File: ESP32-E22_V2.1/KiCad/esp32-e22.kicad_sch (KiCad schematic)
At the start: 32 parts, among them J1 Conn_01x04_Socket, J10 Conn_01x02_Socket, J3 Conn_01x04_Socket, J4 Conn_01x03_Socket, J5 SMA, J6 Conn_01x02_Socket, J7 USB_C_Receptacle_PowerOnly_6P, J8 Conn_01x04_Socket, J9 Conn_01x02_Socket, SW1 SW_Push, U1 E22-40033S, U2 ESP32-DevKitC, U3 DM-OLED096-636

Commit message: new Version 2.0.10 & 2.0.6
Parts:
- removed J7: USB_C_Receptacle_PowerOnly_6P, Connector_USB:USB_C_Receptacle_GCT_USB4125-xx-x-0190_6P_TopMnt_Horizontal, symbol Connector:USB_C_Receptacle_PowerOnly_6P
- added J2: Conn_01x04_Socket, Connector_PinHeader_2.54mm:PinHeader_1x04_P2.54mm_Vertical, symbol Connector:Conn_01x04_Socket
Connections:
- net +5V: now also D2.1 (A1); no longer D2.2 (A2)
- net GND: now also D2.2 (A2), J2.4 (Pin_4); no longer D2.1 (A1)
- net at R2.1: now also J2.2 (Pin_2)
- net at D3.2 (A): now also J2.1 (Pin_1)
- net at R1.1: now also J2.3 (Pin_3)
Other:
- moved on the sheet: D2
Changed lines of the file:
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@@
 		(title "ESP32 - E22 Board")
 		(date "2024-10-04")
-		(rev "V2.0.9")
+		(rev "V2.0.10")
 		(company "DK9BT / OE3WAS")
 	)
@@
 	)
 	(junction
-		(at 31.75 181.61)
-		(diameter 0)
-		(color 0 0 0 0)
-	)
-	(junction
 		(at 81.28 156.21)
 		(diameter 0)
@@
 	)
 	(junction
-		(at 175.26 93.98)
+		(at 86.36 181.61)
 		(diameter 0)
 		(color 0 0 0 0)
 	)
 	(junction
-		(at 99.06 26.67)
+		(at 175.26 93.98)
 		(diameter 0)
 		(color 0 0 0 0)
 	)
 	(junction
-		(at 40.64 181.61)
+		(at 99.06 26.67)
 		(diameter 0)
 		(color 0 0 0 0)
@@
 	(wire
 		(pts
+			(xy 40.64 165.1) (xy 46.99 171.45)
+		)
+		(stroke
+			(width 0)
+			(type default)
+		)
+	)
+	(wire
+		(pts
 			(xy 143.51 165.1) (xy 143.51 168.91)
 		)
@@
 	(wire
 		(pts
-			(xy 49.53 181.61) (xy 40.64 181.61)
+			(xy 25.4 49.53) (xy 35.56 49.53)
 		)
 		(stroke
@@
 	(wire
 		(pts
-			(xy 25.4 49.53) (xy 35.56 49.53)
+			(xy 198.12 55.88) (xy 223.52 55.88)
 		)
 		(stroke
@@
 	(wire
 		(pts
-			(xy 198.12 55.88) (xy 223.52 55.88)
+			(xy 246.38 48.26) (xy 254 48.26)
 		)
 		(stroke
@@
 	(wire
 		(pts
-			(xy 246.38 48.26) (xy 254 48.26)
+			(xy 119.38 156.21) (xy 132.08 156.21)
 		)
 		(stroke
@@
 	(wire
 		(pts
-			(xy 119.38 156.21) (xy 132.08 156.21)
+			(xy 154.94 44.45) (xy 154.94 43.18)
 		)
 		(stroke
@@
 	(wire
 		(pts
-			(xy 154.94 44.45) (xy 154.94 43.18)
+			(xy 128.27 50.8) (xy 190.5 50.8)
 		)
 		(stroke
@@
 	(wire
 		(pts
-			(xy 128.27 50.8) (xy 190.5 50.8)
+			(xy 132.08 168.91) (xy 143.51 168.91)
 		)
 		(stroke
@@
 	(wire
 		(pts
-			(xy 132.08 168.91) (xy 143.51 168.91)
+			(xy 38.1 165.1) (xy 40.64 165.1)
 		)
 		(stroke
@@
 	(wire
 		(pts
+			(xy 38.1 172.72) (xy 46.99 181.61)
+		)
+		(stroke
+			(width 0)
+			(type default)
+		)
+	)
+	(wire
+		(pts
 			(xy 248.92 66.04) (xy 248.92 76.2)
 		)
@@
 	(wire
 		(pts
-			(xy 40.64 181.61) (xy 40.64 184.15)
+			(xy 86.36 181.61) (xy 86.36 182.88)
 		)
 		(stroke
@@
 	(wire
 		(pts
+			(xy 86.36 181.61) (xy 58.42 181.61)
+		)
+		(stroke
+			(width 0)
+			(type default)
+		)
+	)
+	(wire
+		(pts
 			(xy 260.35 58.42) (xy 260.35 60.96)
 		)
@@
 	(wire
 		(pts
-			(xy 24.13 181.61) (xy 31.75 181.61)
+			(xy 46.99 181.61) (xy 49.53 181.61)
 		)
 		(stroke
@@
 	(wire
 		(pts
+			(xy 38.1 162.56) (xy 40.64 162.56)
+		)
+		(stroke
+			(width 0)
+			(type default)
+		)
+	)
+	(wire
+		(pts
 			(xy 128.27 48.26) (xy 195.58 48.26)
 		)
@@
 	(wire
 		(pts
-			(xy 119.38 168.91) (xy 132.08 168.91)
+			(xy 38.1 167.64) (xy 38.1 172.72)
 		)
 		(stroke
@@
 	(wire
 		(pts
-			(xy 246.38 78.74) (xy 248.92 78.74)
+			(xy 119.38 168.91) (xy 132.08 168.91)
 		)
 		(stroke
@@
 	(wire
 		(pts
-			(xy 58.42 181.61) (xy 119.38 181.61)
+			(xy 246.38 78.74) (xy 248.92 78.74)
 		)
 		(stroke
@@
 	(wire
 		(pts
+			(xy 38.1 160.02) (xy 43.18 160.02)
+		)
+		(stroke
+			(width 0)
+			(type default)
+		)
+	)
+	(wire
+		(pts
 			(xy 154.94 44.45) (xy 158.75 44.45)
 		)
@@
 	(wire
 		(pts
+			(xy 86.36 181.61) (xy 119.38 181.61)
+		)
+		(stroke
+			(width 0)
+			(type default)
+		)
+	)
+	(wire
+		(pts
 			(xy 71.12 162.56) (xy 72.39 162.56)
 		)
@@
 	(wire
 		(pts
+			(xy 40.64 162.56) (xy 46.99 168.91)
+		)
+		(stroke
+			(width 0)
+			(type default)
+		)
+	)
+	(wire
+		(pts
 			(xy 220.98 81.28) (xy 220.98 82.55)
 		)
@@
 	(wire
 		(pts
-			(xy 31.75 181.61) (xy 40.64 181.61)
-		)
-		(stroke
-			(width 0)
-			(type default)
-		)
-	)
-	(wire
-		(pts
 			(xy 195.58 66.04) (xy 223.52 66.04)
 		)
@@
 	(wire
 		(pts
+			(xy 43.18 160.02) (xy 46.99 156.21)
+		)
+		(stroke
+			(width 0)
+			(type default)
+		)
+	)
+	(wire
+		(pts
 			(xy 175.26 78.74) (xy 185.42 78.74)
 		)
@@
 	)
 	(symbol
-		(lib_id "Connector:USB_C_Receptacle_PowerOnly_6P")
-		(at 31.75 163.83 0)
-		(unit 1)
-		(exclude_from_sim no)
-		(in_bom yes)
-		(on_board yes)
-		(dnp no)
-		(fields_autoplaced yes)
-		(property "Reference" "J7"
-			(at 31.75 148.59 0)
-			(effects
-				(font
-					(size 1.27 1.27)
-				)
-			)
-		)
-		(property "Value" "USB_C_Receptacle_PowerOnly_6P"
-			(at 31.75 148.59 0)
-			(effects
-				(font
-					(size 1.27 1.27)
-				)
-				(hide yes)
-			)
-		)
-		(property "Footprint" "Connector_USB:USB_C_Receptacle_GCT_USB4125-xx-x-0190_6P_TopMnt_Horizontal"
-			(at 35.56 161.29 0)
-			(effects
-				(font
-					(size 1.27 1.27)
-				)
-				(hide yes)
-			)
-		)
-		(property "Datasheet" "https://www.usb.org/sites/default/files/documents/usb_type-c.zip"
-			(at 31.75 163.83 0)
-			(effects
-				(font
-					(size 1.27 1.27)
-				)
-				(hide yes)
-			)
-		)
-		(property "Description" "USB Power-Only 6P Type-C Receptacle connector"
-			(at 31.75 163.83 0)
-			(effects
-				(font
-					(size 1.27 1.27)
-				)
-				(hide yes)
-			)
-		)
-		(pin "A12"
-		)
-		(pin "S1"
-		)
-		(pin "A9"
-		)
-		(pin "B5"
-		)
-		(pin "B9"
-		)
-		(pin "B12"
-		)
-		(pin "A5"
-		)
-		(instances
-			(project ""
-				(path "/7ac59502-473d-4014-a9ef-f4cf3cefb926"
-					(reference "J7")
-					(unit 1)
-				)
-			)
-		)
-	)
-	(symbol
 		(lib_id "Device:R")
 		(at 30.48 38.1 90)
@@
 	)
 	(symbol
+		(lib_id "Connector:Conn_01x04_Socket")
+		(at 33.02 162.56 0)
+		(mirror y)
+		(unit 1)
+		(exclude_from_sim no)
+		(in_bom yes)
+		(on_board yes)
+		(dnp no)
+		(property "Reference" "J2"
+			(at 34.29 169.926 0)
+			(effects
+				(font
+					(size 1.27 1.27)
+				)
+				(justify left)
+			)
+		)
+		(property "Value" "Conn_01x04_Socket"
+			(at 26.162 165.1 0)
+			(effects
+				(font
+					(size 1.27 1.27)
+				)
+				(justify left)
+				(hide yes)
+			)
+		)
+		(property "Footprint" "Connector_PinHeader_2.54mm:PinHeader_1x04_P2.54mm_Vertical"
+			(at 33.02 162.56 0)
+			(effects
+				(font
+					(size 1.27 1.27)
+				)
+				(hide yes)
+			)
+		)
+		(property "Datasheet" "~"
+			(at 33.02 162.56 0)
+			(effects
+				(font
+					(size 1.27 1.27)
+				)
+				(hide yes)
+			)
+		)
+		(property "Description" "Generic connector, single row, 01x04, script generated"
+			(at 33.02 162.56 0)
+			(effects
+				(font
+					(size 1.27 1.27)
+				)
+				(hide yes)
+			)
+		)
+		(pin "1"
+		)
+		(pin "4"
+		)
+		(pin "3"
+		)
+		(pin "2"
+		)
+		(instances
+			(project "esp32-e22"
+				(path "/7ac59502-473d-4014-a9ef-f4cf3cefb926"
+					(reference "J2")
+					(unit 1)
+				)
+			)
+		)
+	)
+	(symbol
 		(lib_id "power:+3.3V")
 		(at 99.06 26.67 0)
@@
 	(symbol
 		(lib_id "Diode:SD05_SOD323")
-		(at 86.36 162.56 90)
+		(at 86.36 162.56 270)
 		(unit 1)
 		(exclude_from_sim no)
@@
 					(size 1.27 1.27)
 				)
-				(justify right)
+				(justify left)
 			)
 		)
@@
 					(size 1.27 1.27)
 				)
-				(justify right)
+				(justify left)
 			)
 		)
 		(property "Footprint" "Diode_SMD:D_SOD-523"
-			(at 91.44 162.56 0)
+			(at 81.28 162.56 0)
 			(effects
 				(font
@@
 	(symbol
 		(lib_id "power:GND")
-		(at 40.64 184.15 0)
+		(at 86.36 182.88 0)
 		(unit 1)
 		(exclude_from_sim no)
@@
 		(fields_autoplaced yes)
 		(property "Reference" "#PWR021"
-			(at 40.64 190.5 0)
+			(at 86.36 189.23 0)
 			(effects
 				(font
@@
 		)
 		(property "Value" "GND"
-			(at 40.64 189.23 0)
+			(at 86.36 187.96 0)
 			(effects
 				(font
@@
 		)
 		(property "Footprint" ""
-			(at 40.64 184.15 0)
+			(at 86.36 182.88 0)
 			(effects
 				(font
@@
 		)
 		(property "Datasheet" ""
-			(at 40.64 184.15 0)
+			(at 86.36 182.88 0)
 			(effects
 				(font
@@
 		)
 		(property "Description" "Power symbol creates a global label with name \"GND\" , ground"
-			(at 40.64 184.15 0)
+			(at 86.36 182.88 0)
 			(effects
 				(font

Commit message: real update
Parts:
- removed J2: Conn_01x04_Socket, Connector_PinHeader_2.54mm:PinHeader_1x04_P2.54mm_Vertical, symbol Connector:Conn_01x04_Socket
- added C8: 100nF, Capacitor_THT:C_Disc_D4.7mm_W2.5mm_P5.00mm, symbol Device:C_Small
- added J2: ~, footprints:USB-C_vert, symbol USB-C:USB-C_vert
- added R8: 0R, Resistor_SMD:R_0805_2012Metric, symbol Device:R
- J3: renamed from J9; Funktion (none) -> ext. Power 5V DC
- J4: renamed from J1; Funktion (none) -> GPS
- J5: renamed from J4; Funktion (none) -> ONEWIRE
- J6: renamed from J8; Funktion (none) -> I²C
- J7: renamed from J3; Funktion (none) -> I²C
- J8: renamed from J5; Funktion (none) -> Antenne
- renumbered C5 to C1, C6 to C2, C1 to C3, C2 to C4, C3 to C5, C7 to C6, C4 to C7, D3 to D1, D1 to D2, D2 to D3, J10 to J1, J6 to J9, R3 to R1, R4 to R2, R1 to R3, R2 to R4, U2 to U1, U3 to U2, U1 to U3
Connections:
- net +3.3V: now also C8.2
- net GND: now also C8.1, J2.4 (GND)
- net at R3.1: now also J2.3 (CC2)
- net at D1.2 (A): now also J2.1 (V+)
- net at R4.1: now also J2.2 (CC1)
- net at J8.1 (In): now also R8.1; no longer U3.21 (ANT)
- new net: R8.2, U3.21 (ANT)
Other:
- note removed: "BME"
- note removed: "GPS"
- note removed: "ONEWIRE"
- note removed: "ext. Power 5V DC"
- moved on the sheet: J8, J9, R3, R4, U3

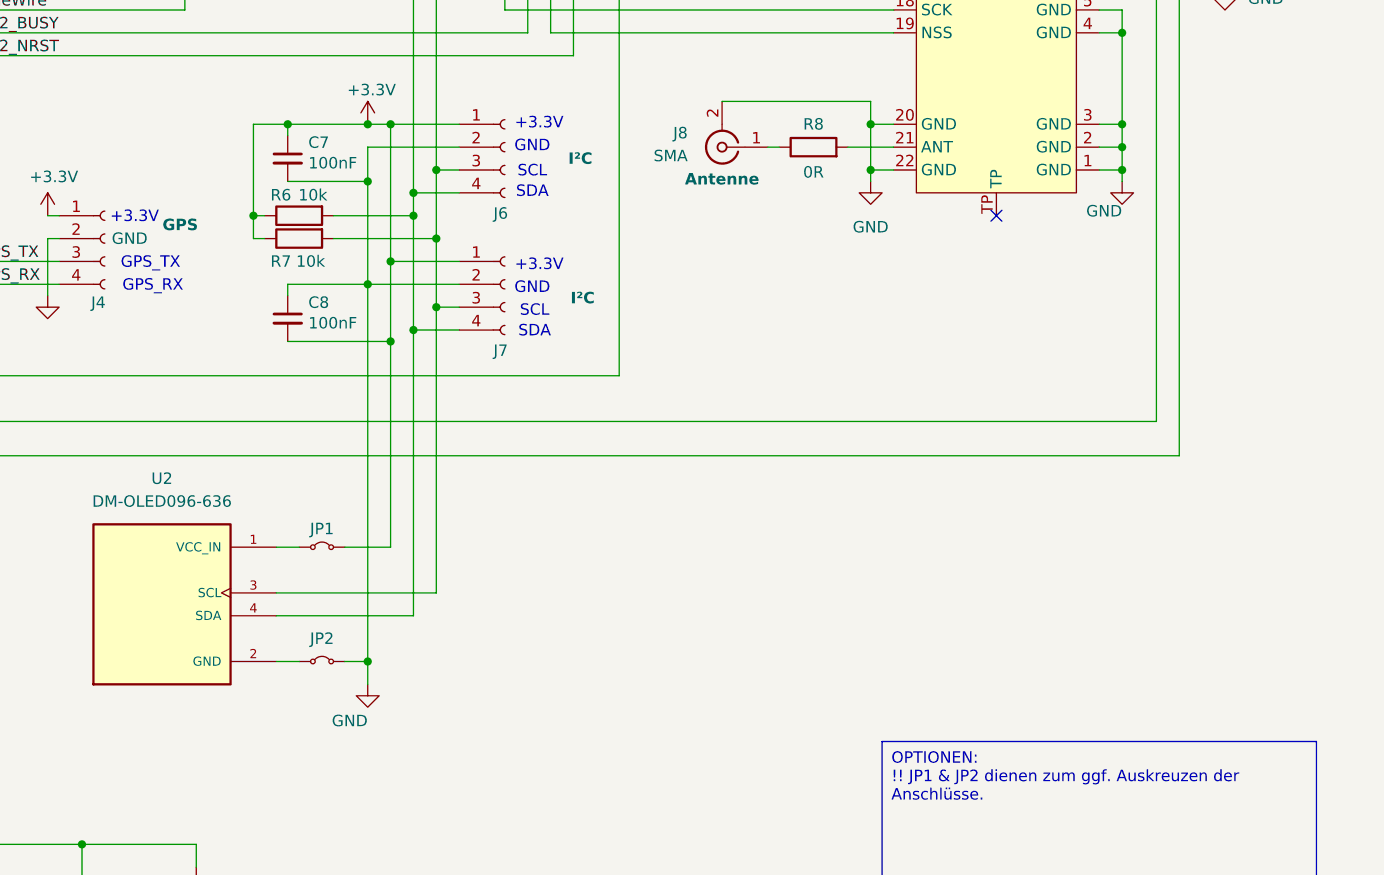
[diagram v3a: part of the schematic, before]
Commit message: corrected footprints symbols and 3d Models for our custom parts
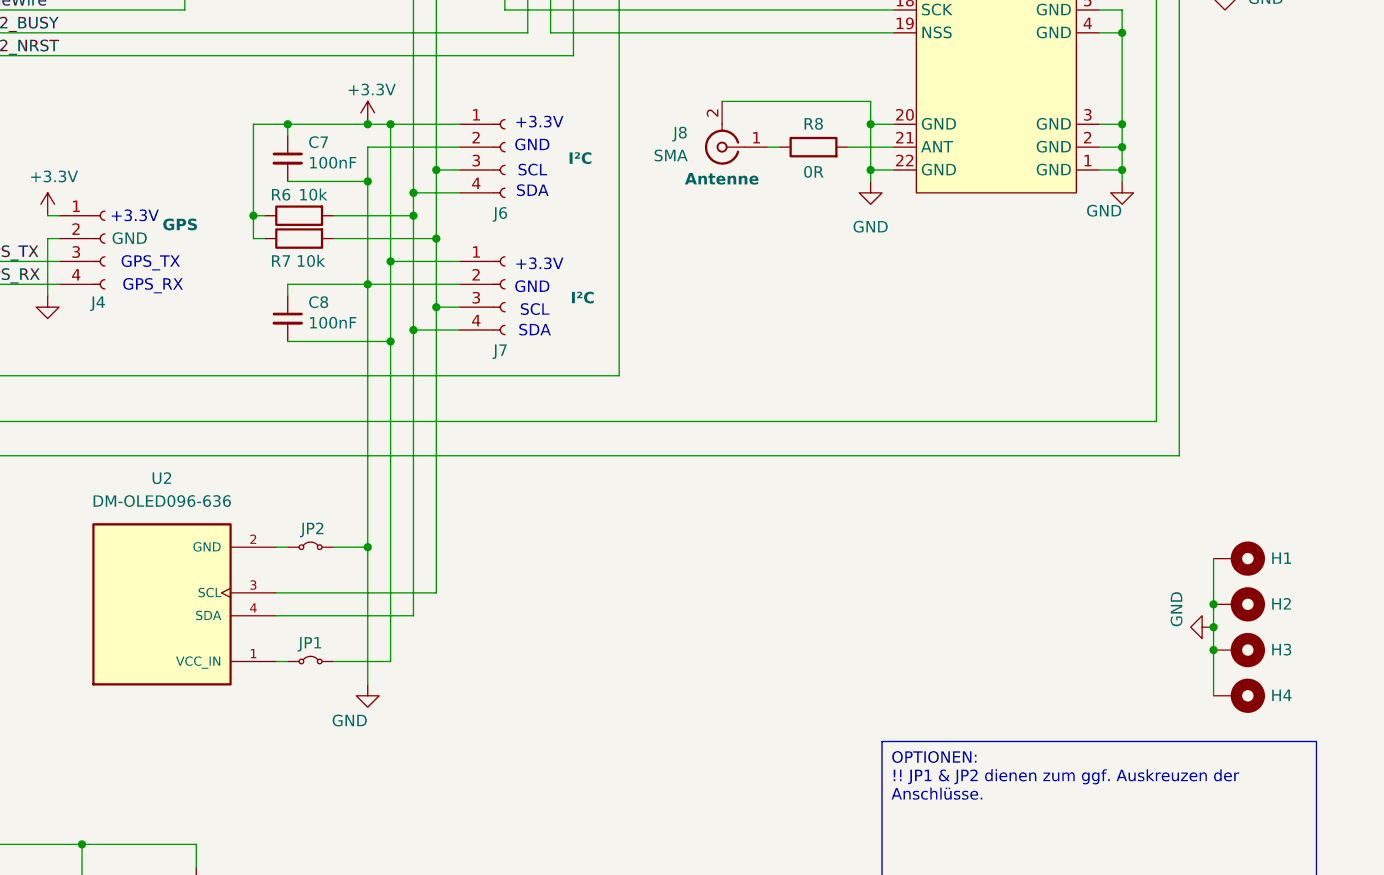
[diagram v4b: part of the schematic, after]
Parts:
- added H1, H2, H3, H4: MountingHole_Pad, MountingHole:MountingHole_2.2mm_M2_Pad_TopBottom, symbol Mechanical:MountingHole_Pad
- J2: footprint footprints:USB-C_vert -> footprints_local:USB-C_vert
- U1: footprint E22:ESP32-DevKitC -> footprints_local:ESP32-DevKitC
- U2: footprint E22:DM-OLED096-636 -> footprints_local:DM-OLED096-636
- U3: footprint E22:E22-400M33S -> footprints_local:E22-400M33S
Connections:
- net GND: now also H1.1, H2.1, H3.1, H4.1
- no-connect marks 17 -> 16
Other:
- moved on the sheet: JP1, JP2

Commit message: some fixes
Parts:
- added NT1: NetTie_2, NetTie:NetTie-2_SMD_Pad0.5mm, symbol NetTie:NetTie_2
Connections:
- net +3.3V: now also JP1.1 (A), U2.1 (VCC_IN)
- net GND: now also NT1.2; no longer JP2.2 (B)
- net at JP2.1 (A), U2.2 (GND): now also JP2.2 (B), NT1.1
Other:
- moved on the sheet: JP2
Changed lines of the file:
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@@
 	)
 	(junction
+		(at 171.45 135.89)
+		(diameter 0)
+		(color 0 0 0 0)
+	)
+	(junction
 		(at 182.88 96.52)
 		(diameter 0)
@@
 	)
 	(junction
+		(at 175.26 123.19)
+		(diameter 0)
+		(color 0 0 0 0)
+	)
+	(junction
 		(at 81.28 156.21)
 		(diameter 0)
@@
 	)
 	(junction
+		(at 165.1 123.19)
+		(diameter 0)
+		(color 0 0 0 0)
+	)
+	(junction
 		(at 180.34 99.06)
 		(diameter 0)
@@
 	)
 	(junction
+		(at 170.18 123.19)
+		(diameter 0)
+		(color 0 0 0 0)
+	)
+	(junction
 		(at 86.36 156.21)
 		(diameter 0)
@@
 	)
 	(junction
+		(at 166.37 135.89)
+		(diameter 0)
+		(color 0 0 0 0)
+	)
+	(junction
 		(at 259.08 66.04)
 		(diameter 0)
@@
 	)
 	(junction
-		(at 175.26 123.19)
-		(diameter 0)
-		(color 0 0 0 0)
-	)
-	(junction
 		(at 269.24 134.62)
 		(diameter 0)
@@
 	(wire
 		(pts
+			(xy 170.18 123.19) (xy 170.18 124.46)
+		)
+		(stroke
+			(width 0)
+			(type default)
+		)
+	)
+	(wire
+		(pts
 			(xy 166.37 93.98) (xy 175.26 93.98)
 		)
@@
 	(wire
 		(pts
+			(xy 171.45 137.16) (xy 171.45 135.89)
+		)
+		(stroke
+			(width 0)
+			(type default)
+		)
+	)
+	(wire
+		(pts
 			(xy 49.53 33.02) (xy 52.07 33.02)
 		)
@@
 	(wire
 		(pts
+			(xy 165.1 124.46) (xy 170.18 124.46)
+		)
+		(stroke
+			(width 0)
+			(type default)
+		)
+	)
+	(wire
+		(pts
 			(xy 81.28 156.21) (xy 86.36 156.21)
 		)
@@
 	(wire
 		(pts
-			(xy 165.1 123.19) (xy 166.37 123.19)
-		)
-		(stroke
-			(width 0)
-			(type default)
-		)
-	)
-	(wire
-		(pts
 			(xy 180.34 83.82) (xy 180.34 86.36)
 		)
@@
 	(wire
 		(pts
+			(xy 175.26 123.19) (xy 175.26 138.43)
+		)
+		(stroke
+			(width 0)
+			(type default)
+		)
+	)
+	(wire
+		(pts
 			(xy 156.21 166.37) (xy 156.21 168.91)
 		)
@@
 	(wire
 		(pts
+			(xy 165.1 123.19) (xy 165.1 124.46)
+		)
+		(stroke
+			(width 0)
+			(type default)
+		)
+	)
+	(wire
+		(pts
 			(xy 36.83 156.21) (xy 49.53 156.21)
 		)
@@
 	(wire
 		(pts
-			(xy 175.26 123.19) (xy 175.26 138.43)
-		)
-		(stroke
-			(width 0)
-			(type default)
-		)
-	)
-	(wire
-		(pts
 			(xy 203.2 50.8) (xy 203.2 104.14)
 		)
@@
 	(wire
 		(pts
-			(xy 171.45 123.19) (xy 175.26 123.19)
-		)
-		(stroke
-			(width 0)
-			(type default)
-		)
-	)
-	(wire
-		(pts
 			(xy 43.18 167.64) (xy 48.26 170.18)
 		)
@@
 	(wire
 		(pts
+			(xy 166.37 135.89) (xy 166.37 137.16)
+		)
+		(stroke
+			(width 0)
+			(type default)
+		)
+	)
+	(wire
+		(pts
 			(xy 195.58 66.04) (xy 233.68 66.04)
 		)
@@
 	(wire
 		(pts
+			(xy 166.37 137.16) (xy 171.45 137.16)
+		)
+		(stroke
+			(width 0)
+			(type default)
+		)
+	)
+	(wire
+		(pts
 			(xy 154.94 35.56) (xy 154.94 31.75)
 		)
@@
 	)
 	(symbol
+		(lib_id "NetTie:NetTie_2")
+		(at 172.72 123.19 0)
+		(unit 1)
+		(exclude_from_sim no)
+		(in_bom no)
+		(on_board yes)
+		(dnp no)
+		(property "Reference" "NT1"
+			(at 170.942 116.586 0)
+			(effects
+				(font
+					(size 1.27 1.27)
+				)
+			)
+		)
+		(property "Value" "NetTie_2"
+			(at 170.688 118.872 0)
+			(effects
+				(font
+					(size 1.27 1.27)
+				)
+			)
+		)
+		(property "Footprint" "NetTie:NetTie-2_SMD_Pad0.5mm"
+			(at 172.72 123.19 0)
+			(effects
+				(font
+					(size 1.27 1.27)
+				)
+				(hide yes)
+			)
+		)
+		(property "Datasheet" "~"
+			(at 172.72 123.19 0)
+			(effects
+				(font
+					(size 1.27 1.27)
+				)
+				(hide yes)
+			)
+		)
+		(property "Description" "Net tie, 2 pins"
+			(at 172.72 123.19 0)
+			(effects
+				(font
+					(size 1.27 1.27)
+				)
+				(hide yes)
+			)
+		)
+		(pin "1"
+		)
+		(pin "2"
+		)
+		(instances
+			(project ""
+				(path "/7ac59502-473d-4014-a9ef-f4cf3cefb926"
+					(reference "NT1")
+					(unit 1)
+				)
+			)
+		)
+	)
+	(symbol
 		(lib_id "power:GND")
 		(at 149.86 34.29 0)
@@
 	(symbol
 		(lib_id "Jumper:Jumper_2_Small_Bridged")
-		(at 168.91 123.19 0)
+		(at 167.64 123.19 0)
 		(unit 1)
 		(exclude_from_sim yes)
@@
 		(dnp no)
 		(property "Reference" "JP2"
-			(at 169.164 121.158 0)
+			(at 167.894 121.158 0)
 			(effects
 				(font
@@
 		)
 		(property "Value" "Jumper_2_Small_Bridged"
-			(at 168.91 120.65 0)
+			(at 167.64 120.65 0)
 			(effects
 				(font
@@
 		)
 		(property "Footprint" "TestPoint:TestPoint_2Pads_Pitch2.54mm_Drill0.8mm"
-			(at 168.91 123.19 0)
+			(at 167.64 123.19 0)
 			(effects
 				(font
@@
 		)
 		(property "Datasheet" "~"
-			(at 168.91 123.19 0)
+			(at 167.64 123.19 0)
 			(effects
 				(font
@@
 		)
 		(property "Description" "Jumper, 2-pole, small symbol, bridged"
-			(at 168.91 123.19 0)
+			(at 167.64 123.19 0)
 			(effects
 				(font

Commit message: update
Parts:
- J2: Funktion (none) -> USB-C
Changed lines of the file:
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@@
 					(size 1.27 1.27)
 				)
+				(hide yes)
 			)
 		)
@@
 					(size 1.27 1.27)
 				)
+				(hide yes)
 			)
 		)
@@
 		(on_board yes)
 		(dnp no)
-		(fields_autoplaced yes)
 		(property "Reference" "J2"
-			(at 30.48 149.86 0)
+			(at 29.972 149.86 0)
 			(effects
 				(font
@@
 			)
 		)
+		(property "Funktion" "USB-C"
+			(at 30.48 152.146 0)
+			(effects
+				(font
+					(size 1.27 1.27)
+					(thickness 0.254)
+					(bold yes)
+				)
+			)
+		)
